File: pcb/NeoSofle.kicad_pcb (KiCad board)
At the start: 2 copper layers, 141.3 x 117.6 mm, 71 parts, among them J1 JST_ACH_BM02B-ACHSS-GAN-ETF_S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, SW1 CPG135001S30, SW10 CPG135001S30, SW11 CPG135001S30, SW12 CPG135001S30, SW13 CPG135001S30, SW14 CPG135001S30, SW15 CPG135001S30, SW16 CPG135001S30, SW17 CPG135001S30, SW18 CPG135001S30, SW19 CPG135001S30, SW2 CPG135001S30, SW20 CPG135001S30, SW21 CPG135001S30, SW22 CPG135001S30, SW23 CPG135001S30, SW24 CPG135001S30, SW25 RotaryEncoder_Switch, SW26 CPG135001S30, SW27 CPG135001S30, SW28 CPG135001S30, SW29 CPG135001S30, SW3 CPG135001S30, SW30 CPG135001S30, SW4 CPG135001S30, SW5 CPG135001S30, SW6 CPG135001S30, SW7 CPG135001S30, SW8 CPG135001S30, SW9 CPG135001S30, U1 nice!nano v2

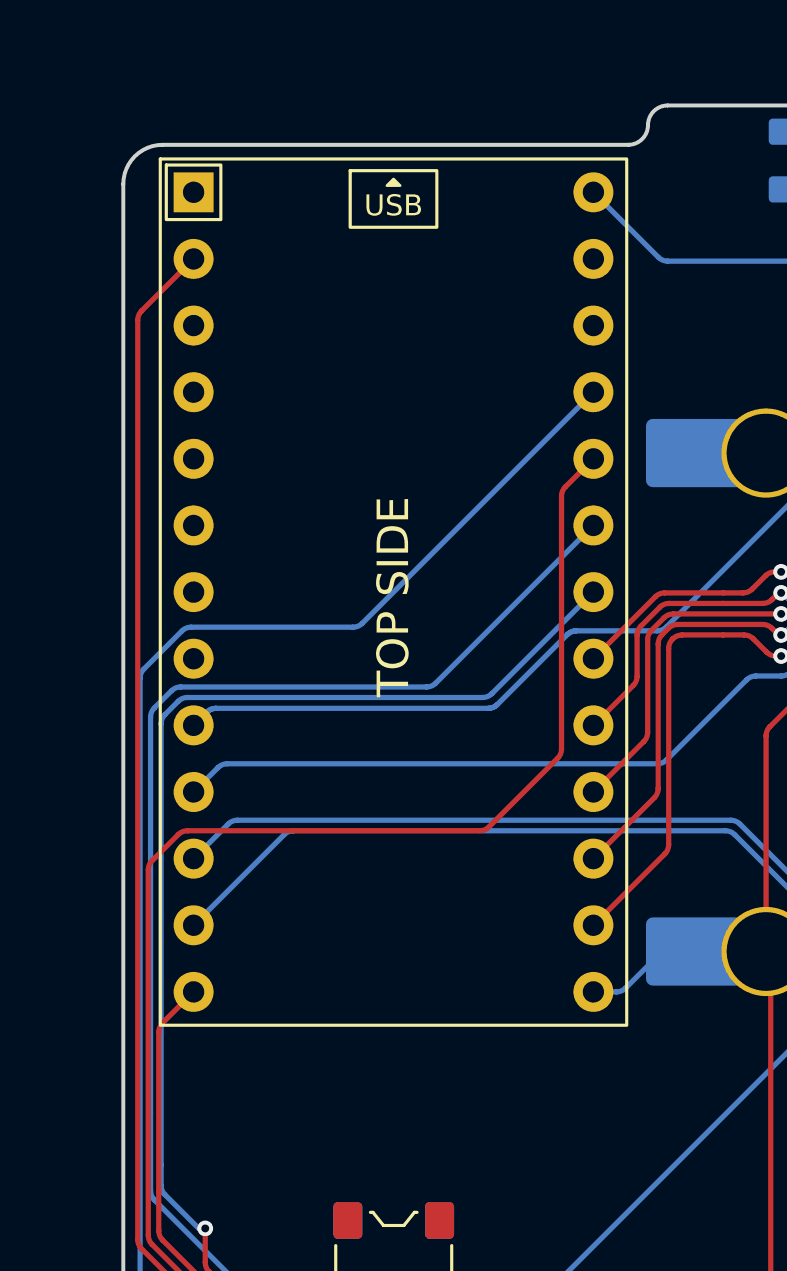
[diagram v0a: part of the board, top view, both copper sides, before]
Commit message: Add edge cutout for battery JST wire, enabling position battery on either side of PCB.
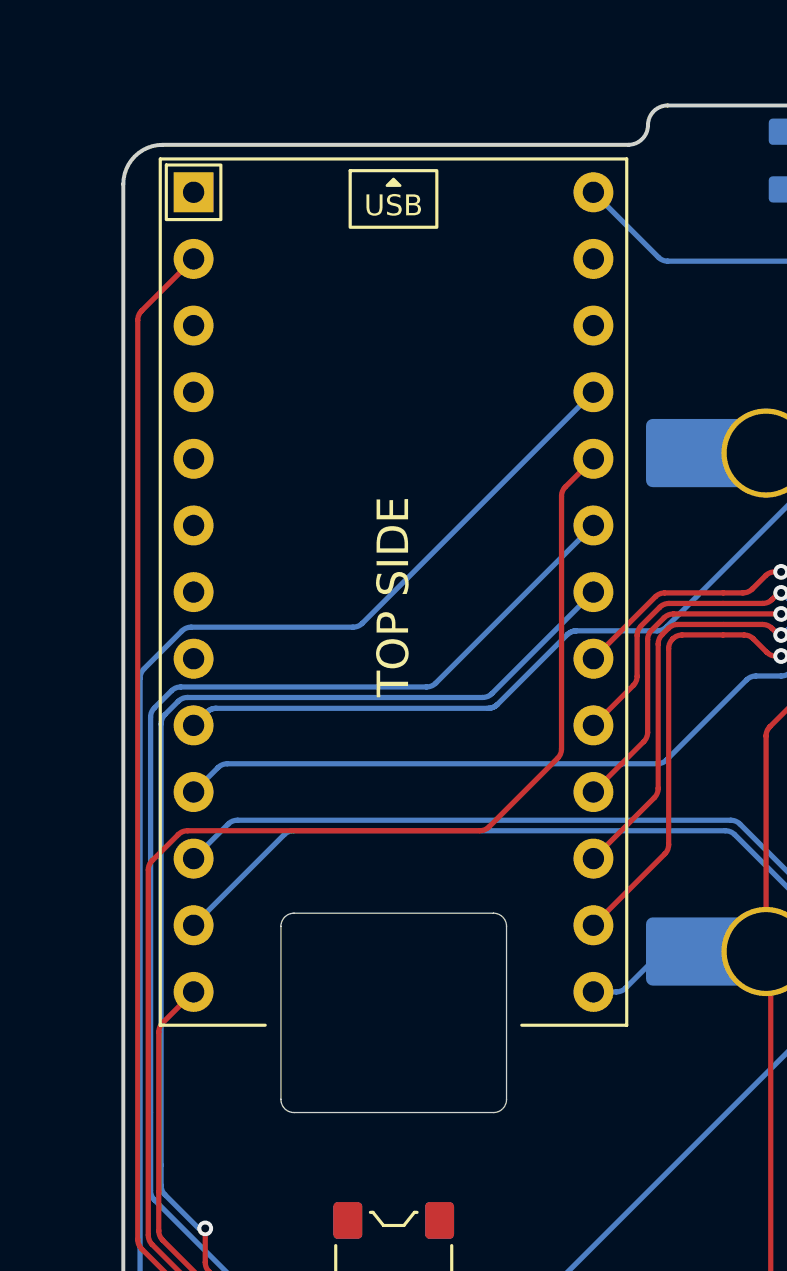
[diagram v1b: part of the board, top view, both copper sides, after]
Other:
- outline, holes or cut-outs redrawn
